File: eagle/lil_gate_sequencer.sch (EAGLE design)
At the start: 69 parts, among them IC1 4093N, IC2 4017N, Q1 2N3904, Q2 2N3904

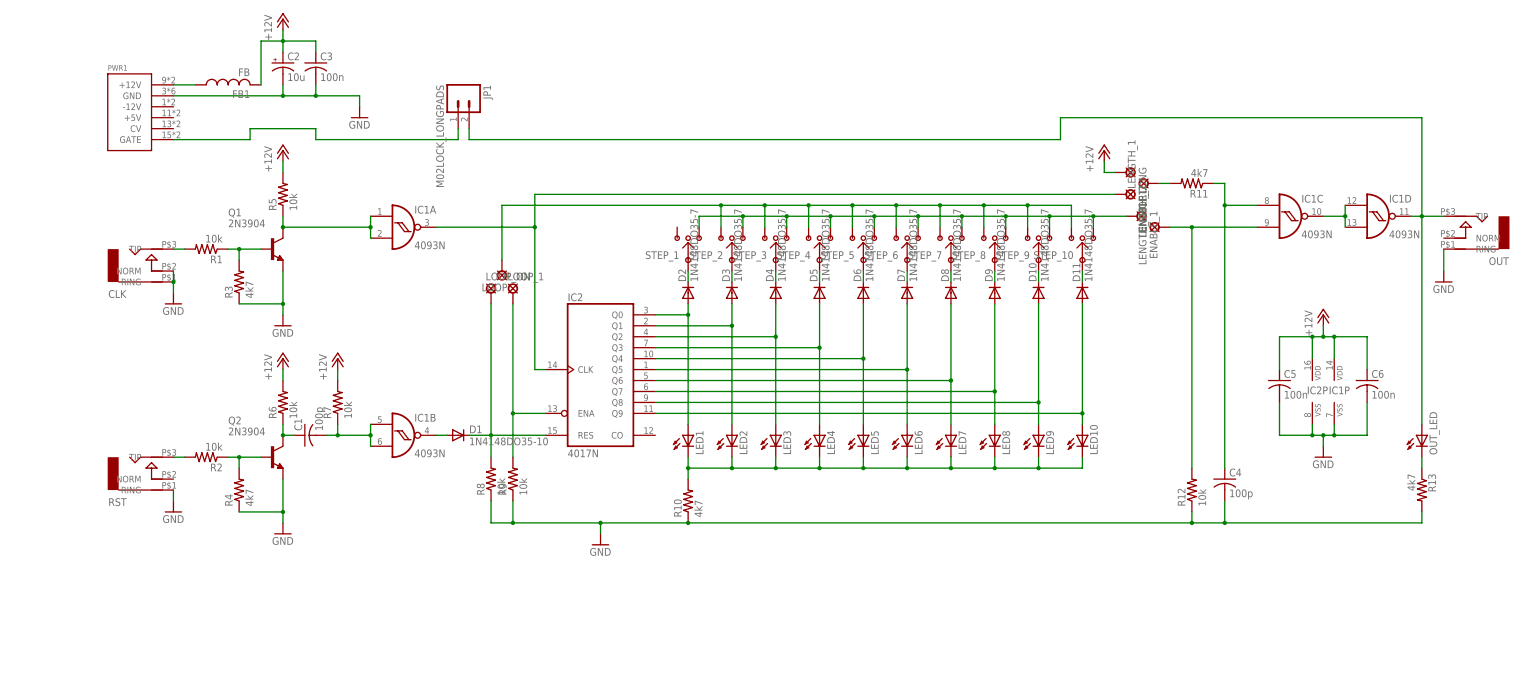
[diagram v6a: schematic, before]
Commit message: normalled gate to reset and added reset to panel
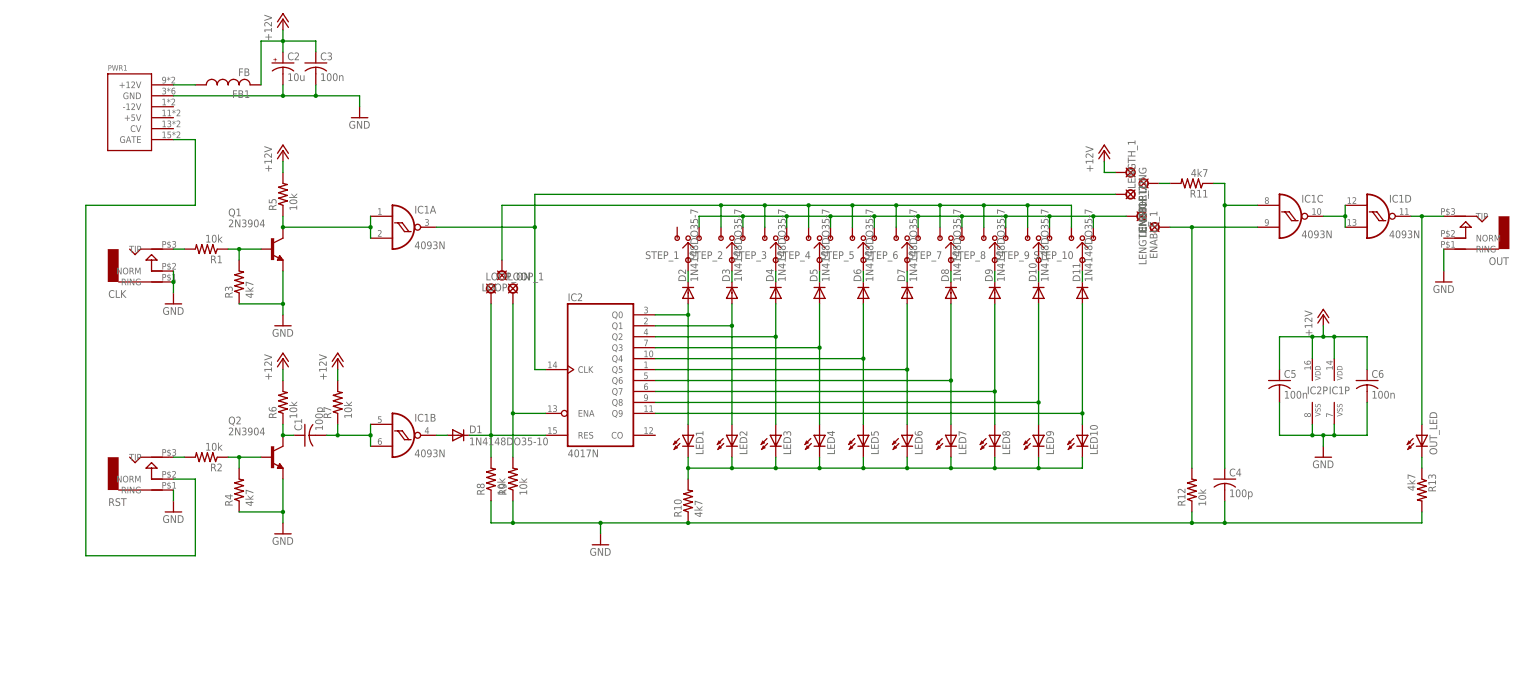
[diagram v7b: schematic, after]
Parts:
- removed JP1: M02LOCK_LONGPADS, SparkFun-Connectors:M02LOCK_LONGPADS
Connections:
- net N$39: now also RST.NORM; no longer JP1.1
- net N$6: no longer JP1.2
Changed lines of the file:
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@@
 <grid distance="0.1" unitdist="inch" unit="inch" style="lines" multiple="1" display="no" altdistance="0.01" altunitdist="inch" altunit="inch"/>
 <layers>
-<layer number="1" name="Top" color="4" fill="1" visible="yes" active="no"/>
-<layer number="16" name="Bottom" color="1" fill="1" visible="yes" active="no"/>
-<layer number="17" name="Pads" color="2" fill="1" visible="yes" active="no"/>
-<layer number="18" name="Vias" color="2" fill="1" visible="yes" active="no"/>
-<layer number="19" name="Unrouted" color="6" fill="1" visible="yes" active="no"/>
-<layer number="20" name="Dimension" color="15" fill="1" visible="yes" active="no"/>
-<layer number="21" name="tPlace" color="7" fill="1" visible="yes" active="no"/>
-<layer number="22" name="bPlace" color="7" fill="1" visible="yes" active="no"/>
-<layer number="23" name="tOrigins" color="15" fill="1" visible="yes" active="no"/>
-<layer number="24" name="bOrigins" color="15" fill="1" visible="yes" active="no"/>
-<layer number="25" name="tNames" color="7" fill="1" visible="yes" active="no"/>
-<layer number="26" name="bNames" color="7" fill="1" visible="yes" active="no"/>
-<layer number="27" name="tValues" color="7" fill="1" visible="yes" active="no"/>
-<layer number="28" name="bValues" color="7" fill="1" visible="yes" active="no"/>
+<layer number="1" name="Top" color="4" fill="1" visible="no" active="no"/>
+<layer number="16" name="Bottom" color="1" fill="1" visible="no" active="no"/>
+<layer number="17" name="Pads" color="2" fill="1" visible="no" active="no"/>
+<layer number="18" name="Vias" color="2" fill="1" visible="no" active="no"/>
+<layer number="19" name="Unrouted" color="6" fill="1" visible="no" active="no"/>
+<layer number="20" name="Dimension" color="15" fill="1" visible="no" active="no"/>
+<layer number="21" name="tPlace" color="7" fill="1" visible="no" active="no"/>
+<layer number="22" name="bPlace" color="7" fill="1" visible="no" active="no"/>
+<layer number="23" name="tOrigins" color="15" fill="1" visible="no" active="no"/>
+<layer number="24" name="bOrigins" color="15" fill="1" visible="no" active="no"/>
+<layer number="25" name="tNames" color="7" fill="1" visible="no" active="no"/>
+<layer number="26" name="bNames" color="7" fill="1" visible="no" active="no"/>
+<layer number="27" name="tValues" color="7" fill="1" visible="no" active="no"/>
+<layer number="28" name="bValues" color="7" fill="1" visible="no" active="no"/>
 <layer number="29" name="tStop" color="7" fill="3" visible="no" active="no"/>
 <layer number="30" name="bStop" color="7" fill="6" visible="no" active="no"/>
@@
 <layer number="35" name="tGlue" color="7" fill="4" visible="no" active="no"/>
 <layer number="36" name="bGlue" color="7" fill="5" visible="no" active="no"/>
-<layer number="37" name="tTest" color="7" fill="1" visible="yes" active="no"/>
-<layer number="38" name="bTest" color="7" fill="1" visible="yes" active="no"/>
+<layer number="37" name="tTest" color="7" fill="1" visible="no" active="no"/>
+<layer number="38" name="bTest" color="7" fill="1" visible="no" active="no"/>
 <layer number="39" name="tKeepout" color="4" fill="11" visible="no" active="no"/>
 <layer number="40" name="bKeepout" color="1" fill="11" visible="no" active="no"/>
@@
 <layer number="44" name="Drills" color="7" fill="1" visible="no" active="no"/>
 <layer number="45" name="Holes" color="7" fill="1" visible="no" active="no"/>
-<layer number="46" name="Milling" color="3" fill="1" visible="yes" active="no"/>
-<layer number="47" name="Measures" color="7" fill="1" visible="yes" active="no"/>
-<layer number="48" name="Document" color="7" fill="1" visible="yes" active="no"/>
-<layer number="49" name="Reference" color="7" fill="1" visible="yes" active="no"/>
-<layer number="50" name="dxf" color="7" fill="1" visible="yes" active="no"/>
-<layer number="51" name="tDocu" color="7" fill="1" visible="yes" active="no"/>
-<layer number="52" name="bDocu" color="7" fill="1" visible="yes" active="no"/>
-<layer number="53" name="tGND_GNDA" color="7" fill="9" visible="yes" active="no"/>
-<layer number="54" name="bGND_GNDA" color="1" fill="9" visible="yes" active="no"/>
-<layer number="56" name="wert" color="7" fill="1" visible="yes" active="no"/>
-<layer number="57" name="tCAD" color="7" fill="1" visible="yes" active="no"/>
-<layer number="59" name="tCarbon" color="7" fill="1" visible="yes" active="no"/>
-<layer number="60" name="bCarbon" color="7" fill="1" visible="yes" active="no"/>
+<layer number="46" name="Milling" color="3" fill="1" visible="no" active="no"/>
+<layer number="47" name="Measures" color="7" fill="1" visible="no" active="no"/>
+<layer number="48" name="Document" color="7" fill="1" visible="no" active="no"/>
+<layer number="49" name="Reference" color="7" fill="1" visible="no" active="no"/>
+<layer number="50" name="dxf" color="7" fill="1" visible="no" active="no"/>
+<layer number="51" name="tDocu" color="7" fill="1" visible="no" active="no"/>
+<layer number="52" name="bDocu" color="7" fill="1" visible="no" active="no"/>
+<layer number="53" name="tGND_GNDA" color="7" fill="9" visible="no" active="no"/>
+<layer number="54" name="bGND_GNDA" color="1" fill="9" visible="no" active="no"/>
+<layer number="56" name="wert" color="7" fill="1" visible="no" active="no"/>
+<layer number="57" name="tCAD" color="7" fill="1" visible="no" active="no"/>
+<layer number="59" name="tCarbon" color="7" fill="1" visible="no" active="no"/>
+<layer number="60" name="bCarbon" color="7" fill="1" visible="no" active="no"/>
 <layer number="90" name="Modules" color="5" fill="1" visible="yes" active="yes"/>
 <layer number="91" name="Nets" color="2" fill="1" visible="yes" active="yes"/>
@@
 <part name="LENGTH_LONG" library="solpad" deviceset="LSP11" device=""/>
 <part name="LENGTH_SHORT" library="solpad" deviceset="LSP11" device=""/>
-<part name="JP1" library="SparkFun-Connectors" deviceset="M02" device="LOCK_LONGPADS"/>
 <part name="OUT_LED" library="led" deviceset="LED" device="5MM"/>
 </parts>
@@
 <instance part="LENGTH_LONG" gate="1" x="243.84" y="116.84" rot="R270"/>
 <instance part="LENGTH_SHORT" gate="1" x="243.84" y="111.76" rot="R270"/>
-<instance part="JP1" gate="G$1" x="88.9" y="134.62" rot="R270"/>
 <instance part="OUT_LED" gate="G$1" x="312.42" y="55.88"/>
 </instances>
@@
 <junction x="312.42" y="106.68"/>
 <pinref part="IC1" gate="D" pin="O"/>
-<pinref part="JP1" gate="G$1" pin="2"/>
-<wire x1="91.44" y1="127" x2="91.44" y2="124.46" width="0.1524" layer="91"/>
-<wire x1="91.44" y1="124.46" x2="228.6" y2="124.46" width="0.1524" layer="91"/>
-<wire x1="228.6" y1="124.46" x2="228.6" y2="129.54" width="0.1524" layer="91"/>
-<wire x1="228.6" y1="129.54" x2="312.42" y2="129.54" width="0.1524" layer="91"/>
-<wire x1="312.42" y1="129.54" x2="312.42" y2="106.68" width="0.1524" layer="91"/>
 <pinref part="OUT_LED" gate="G$1" pin="A"/>
 </segment>
@@
 <segment>
 <pinref part="PWR1" gate="G$1" pin="GATE"/>
-<wire x1="22.86" y1="124.46" x2="40.64" y2="124.46" width="0.1524" layer="91"/>
-<wire x1="40.64" y1="124.46" x2="40.64" y2="127" width="0.1524" layer="91"/>
-<wire x1="40.64" y1="127" x2="55.88" y2="127" width="0.1524" layer="91"/>
-<wire x1="55.88" y1="127" x2="55.88" y2="124.46" width="0.1524" layer="91"/>
-<pinref part="JP1" gate="G$1" pin="1"/>
-<wire x1="55.88" y1="124.46" x2="88.9" y2="124.46" width="0.1524" layer="91"/>
-<wire x1="88.9" y1="124.46" x2="88.9" y2="127" width="0.1524" layer="91"/>
-</segment>
-</net>
+<wire x1="22.86" y1="124.46" x2="27.94" y2="124.46" width="0.1524" layer="91"/>
+<wire x1="27.94" y1="124.46" x2="27.94" y2="109.22" width="0.1524" layer="91"/>
+<wire x1="27.94" y1="109.22" x2="2.54" y2="109.22" width="0.1524" layer="91"/>
+<wire x1="2.54" y1="109.22" x2="2.54" y2="27.94" width="0.1524" layer="91"/>
+<wire x1="2.54" y1="27.94" x2="27.94" y2="27.94" width="0.1524" layer="91"/>
+<wire x1="27.94" y1="27.94" x2="27.94" y2="45.72" width="0.1524" layer="91"/>
+<pinref part="RST" gate="G$1" pin="NORM"/>
+<wire x1="27.94" y1="45.72" x2="22.86" y2="45.72" width="0.1524" layer="91"/>
+</segment>
+</net>
